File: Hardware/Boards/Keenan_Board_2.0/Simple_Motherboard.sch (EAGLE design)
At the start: 109 parts, among them J1 AVR_SPI_PRG_6PTH, U1 WIZ811MJ, U1_MUX 74HC4052D,653, U2 ATMEGA328P_PDIP, U2_MUX 74HC4052D,653, U3_MUX 74HC4052D,653, U4_MUX 74HC4052D,653, U5_MUX 74HC4052D,653, U7_MUX 74HC4052D,653, Y1 16MHz

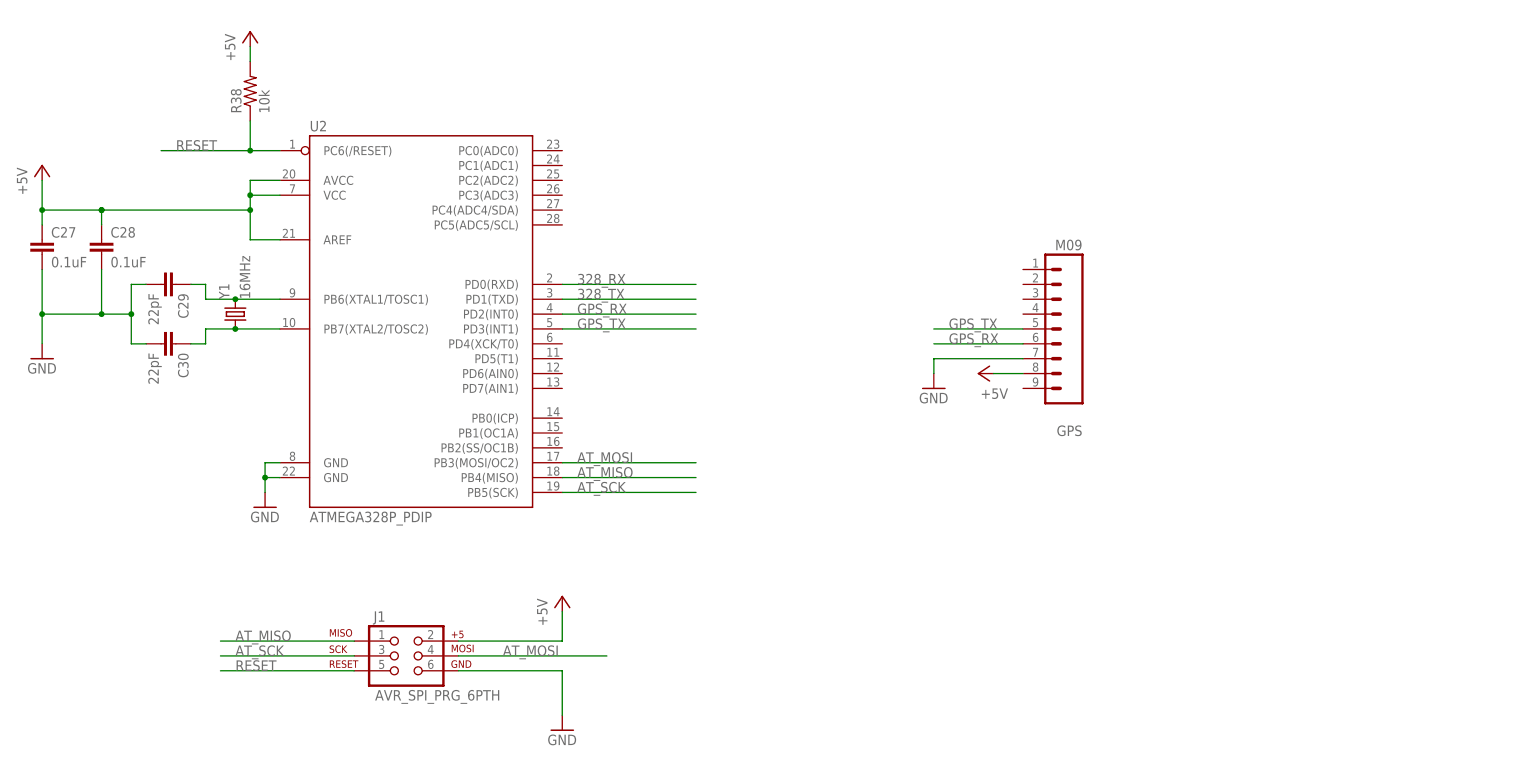
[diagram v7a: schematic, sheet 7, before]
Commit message: Added Bluetooth to schematic
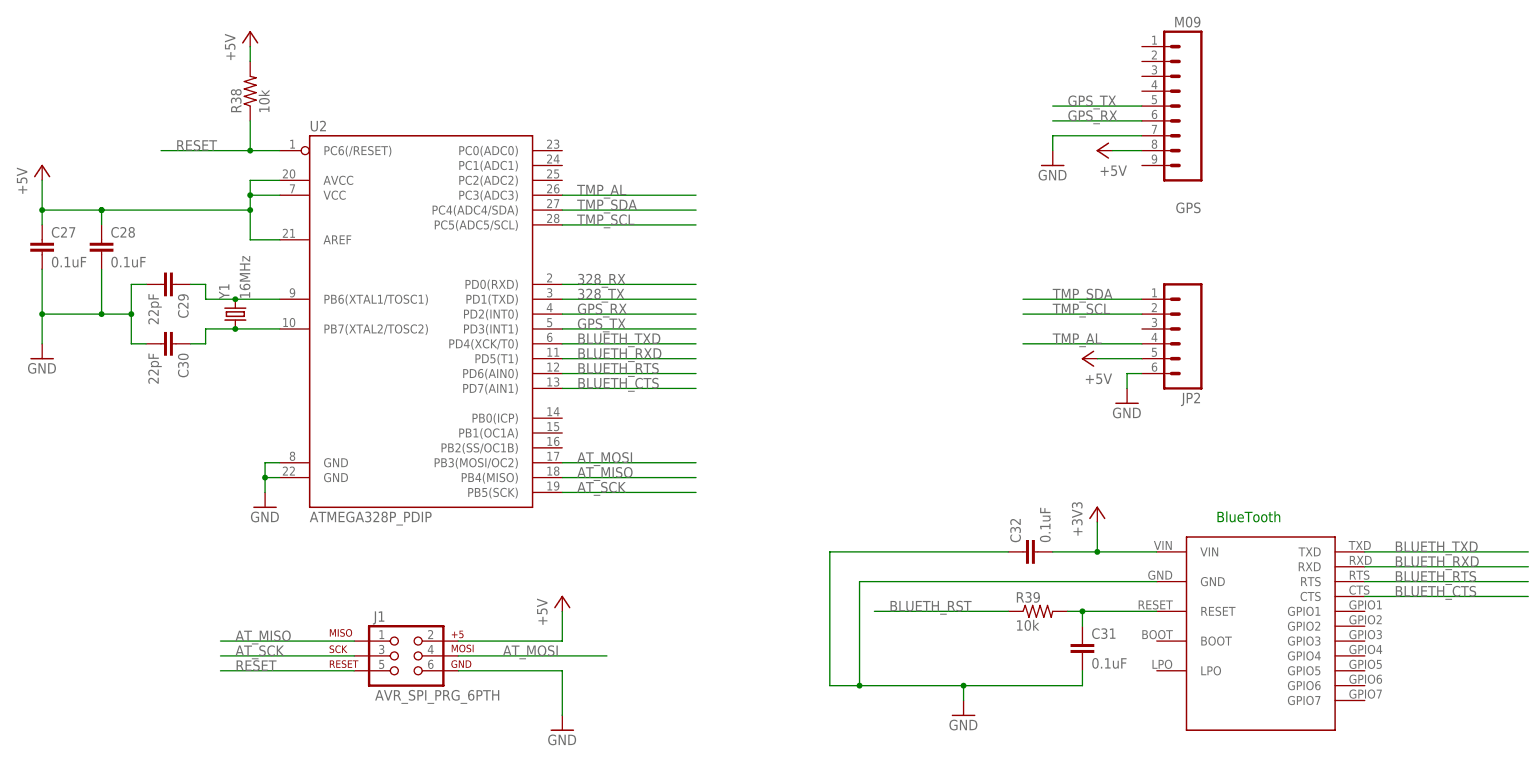
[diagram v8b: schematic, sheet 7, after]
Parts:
- added BLUETOOTH: SPBT2632C2A, SPBT2632C2A:SPBT2632C2A
- added C31, C32: 0.1uF, SparkFun-Passives:CAP1206
- added JP2: (no value), SparkFun-Connectors:M06LONGPADS
- added R39: 10k, SparkFun-Passives:RESISTOR1206
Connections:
- new net BLUETH_CTS: BLUETOOTH.CTS, U2.PD7(AIN1)
- new net BLUETH_RST: R39.1
- new net BLUETH_RTS: BLUETOOTH.RTS, U2.PD6(AIN0)
- new net BLUETH_RXD: BLUETOOTH.RXD, U2.PD5(T1)
- new net BLUETH_TXD: BLUETOOTH.TXD, U2.PD4(XCK/T0)
- new net N$58: BLUETOOTH.RESET, C31.1, R39.2
- new net TMP_AL: JP2.4, U2.PC3(ADC3)
- new net TMP_SCL: JP2.2, U2.PC5(ADC5/SCL)
- new net TMP_SDA: JP2.1, U2.PC4(ADC4/SDA)
- net +3V3: now also BLUETOOTH.VIN, C32.2
- net +5V: now also JP2.5
- net GND: now also BLUETOOTH.GND, C31.2, C32.1, JP2.6
- net GPS_RX: now also U5_MUX.2Y3
- net GPS_TX: now also U5_MUX.1Y3
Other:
- note added: "BlueTooth"
- moved on the sheet: GPS
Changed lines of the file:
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@@
 <part name="P+31" library="supply1" deviceset="+5V" device=""/>
 <part name="GND36" library="supply1" deviceset="GND" device=""/>
+<part name="JP2" library="SparkFun-Connectors" deviceset="M06" device="LONGPADS"/>
+<part name="GND37" library="supply1" deviceset="GND" device=""/>
+<part name="P+32" library="supply1" deviceset="+5V" device=""/>
+<part name="BLUETOOTH" library="SPBT2632C2A" deviceset="SPBT2632C2A" device=""/>
+<part name="GND38" library="supply1" deviceset="GND" device=""/>
+<part name="+3V33" library="supply1" deviceset="+3V3" device=""/>
+<part name="C31" library="SparkFun-Passives" deviceset="CAP" device="1206" value="0.1uF"/>
+<part name="R39" library="SparkFun-Passives" deviceset="RESISTOR" device="1206" value="10k"/>
+<part name="C32" library="SparkFun-Passives" deviceset="CAP" device="1206" value="0.1uF"/>
 </parts>
 <sheets>
@@
 </segment>
 </net>
+<net name="GPS_RX" class="0">
+<segment>
+<pinref part="U5_MUX" gate="A" pin="2Y3"/>
+<wire x1="17.78" y1="-43.18" x2="38.1" y2="-43.18" width="0.1524" layer="91"/>
+<label x="20.32" y="-43.18" size="1.778" layer="95"/>
+</segment>
+</net>
+<net name="GPS_TX" class="0">
+<segment>
+<pinref part="U5_MUX" gate="A" pin="1Y3"/>
+<wire x1="17.78" y1="-30.48" x2="38.1" y2="-30.48" width="0.1524" layer="91"/>
+<label x="20.32" y="-30.48" size="1.778" layer="95"/>
+</segment>
+</net>
 </nets>
 </sheet>
@@
 <description>Sensors</description>
 <plain>
+<text x="137.16" y="-38.1" size="1.778" layer="91">BlueTooth</text>
 </plain>
 <instances>
@@
 <instance part="P+30" gate="1" x="25.4" y="-50.8"/>
 <instance part="GND35" gate="1" x="25.4" y="-73.66"/>
-<instance part="GPS" gate="G$1" x="114.3" y="-5.08" rot="R180"/>
-<instance part="P+31" gate="1" x="96.52" y="-12.7" rot="R90"/>
-<instance part="GND36" gate="1" x="88.9" y="-15.24"/>
+<instance part="GPS" gate="G$1" x="134.62" y="33.02" rot="R180"/>
+<instance part="P+31" gate="1" x="116.84" y="25.4" rot="R90"/>
+<instance part="GND36" gate="1" x="109.22" y="22.86"/>
+<instance part="JP2" gate="G$1" x="129.54" y="-5.08" rot="R180"/>
+<instance part="GND37" gate="1" x="121.92" y="-17.78"/>
+<instance part="P+32" gate="1" x="114.3" y="-10.16" rot="R90"/>
+<instance part="BLUETOOTH" gate="G$1" x="144.78" y="-55.88"/>
+<instance part="GND38" gate="1" x="93.98" y="-71.12"/>
+<instance part="+3V33" gate="G$1" x="116.84" y="-35.56"/>
+<instance part="C31" gate="G$1" x="114.3" y="-60.96"/>
+<instance part="R39" gate="G$1" x="106.68" y="-53.34"/>
+<instance part="C32" gate="G$1" x="106.68" y="-43.18" rot="R90"/>
 </instances>
 <busses>
@@
 <segment>
 <pinref part="GND36" gate="1" pin="GND"/>
-<wire x1="88.9" y1="-12.7" x2="88.9" y2="-10.16" width="0.1524" layer="91"/>
+<wire x1="109.22" y1="25.4" x2="109.22" y2="27.94" width="0.1524" layer="91"/>
 <pinref part="GPS" gate="G$1" pin="7"/>
-<wire x1="88.9" y1="-10.16" x2="104.14" y2="-10.16" width="0.1524" layer="91"/>
+<wire x1="109.22" y1="27.94" x2="124.46" y2="27.94" width="0.1524" layer="91"/>
+</segment>
+<segment>
+<pinref part="JP2" gate="G$1" pin="6"/>
+<pinref part="GND37" gate="1" pin="GND"/>
+<wire x1="124.46" y1="-12.7" x2="121.92" y2="-12.7" width="0.1524" layer="91"/>
+<wire x1="121.92" y1="-12.7" x2="121.92" y2="-15.24" width="0.1524" layer="91"/>
+</segment>
+<segment>
+<pinref part="BLUETOOTH" gate="G$1" pin="GND"/>
+<wire x1="127" y1="-48.26" x2="76.2" y2="-48.26" width="0.1524" layer="91"/>
+<wire x1="76.2" y1="-48.26" x2="76.2" y2="-66.04" width="0.1524" layer="91"/>
+<pinref part="C31" gate="G$1" pin="2"/>
+<wire x1="114.3" y1="-63.5" x2="114.3" y2="-66.04" width="0.1524" layer="91"/>
+<wire x1="114.3" y1="-66.04" x2="93.98" y2="-66.04" width="0.1524" layer="91"/>
+<pinref part="GND38" gate="1" pin="GND"/>
+<wire x1="93.98" y1="-66.04" x2="76.2" y2="-66.04" width="0.1524" layer="91"/>
+<wire x1="93.98" y1="-68.58" x2="93.98" y2="-66.04" width="0.1524" layer="91"/>
+<junction x="93.98" y="-66.04"/>
+<pinref part="C32" gate="G$1" pin="1"/>
+<wire x1="101.6" y1="-43.18" x2="71.12" y2="-43.18" width="0.1524" layer="91"/>
+<wire x1="71.12" y1="-43.18" x2="71.12" y2="-66.04" width="0.1524" layer="91"/>
+<wire x1="71.12" y1="-66.04" x2="76.2" y2="-66.04" width="0.1524" layer="91"/>
+<junction x="76.2" y="-66.04"/>
 </segment>
 </net>
@@
 <pinref part="P+31" gate="1" pin="+5V"/>
 <pinref part="GPS" gate="G$1" pin="8"/>
-<wire x1="99.06" y1="-12.7" x2="104.14" y2="-12.7" width="0.1524" layer="91"/>
+<wire x1="119.38" y1="25.4" x2="124.46" y2="25.4" width="0.1524" layer="91"/>
+</segment>
+<segment>
+<pinref part="P+32" gate="1" pin="+5V"/>
+<pinref part="JP2" gate="G$1" pin="5"/>
+<wire x1="116.84" y1="-10.16" x2="124.46" y2="-10.16" width="0.1524" layer="91"/>
 </segment>
 </net>
@@
 <segment>
 <pinref part="GPS" gate="G$1" pin="6"/>
-<wire x1="104.14" y1="-7.62" x2="88.9" y2="-7.62" width="0.1524" layer="91"/>
-<label x="91.44" y="-7.62" size="1.778" layer="95"/>
+<wire x1="124.46" y1="30.48" x2="109.22" y2="30.48" width="0.1524" layer="91"/>
+<label x="111.76" y="30.48" size="1.778" layer="95"/>
 </segment>
 <segment>
@@
 <segment>
 <pinref part="GPS" gate="G$1" pin="5"/>
-<wire x1="104.14" y1="-5.08" x2="88.9" y2="-5.08" width="0.1524" layer="91"/>
-<label x="91.44" y="-5.08" size="1.778" layer="95"/>
+<wire x1="124.46" y1="33.02" x2="109.22" y2="33.02" width="0.1524" layer="91"/>
+<label x="111.76" y="33.02" size="1.778" layer="95"/>
 </segment>
 <segment>
@@
 </segment>
 </net>
+<net name="TMP_SDA" class="0">
+<segment>
+<pinref part="JP2" gate="G$1" pin="1"/>
+<wire x1="124.46" y1="0" x2="104.14" y2="0" width="0.1524" layer="91"/>
+<label x="109.22" y="0" size="1.778" layer="95"/>
+</segment>
+<segment>
+<pinref part="U2" gate="G$1" pin="PC4(ADC4/SDA)"/>
+<wire x1="25.4" y1="15.24" x2="48.26" y2="15.24" width="0.1524" layer="91"/>
+<label x="27.94" y="15.24" size="1.778" layer="95"/>
+</segment>
+</net>
+<net name="TMP_AL" class="0">
+<segment>
+<pinref part="JP2" gate="G$1" pin="4"/>
+<wire x1="124.46" y1="-7.62" x2="104.14" y2="-7.62" width="0.1524" layer="91"/>
+<label x="109.22" y="-7.62" size="1.778" layer="95"/>
+</segment>
+<segment>
+<pinref part="U2" gate="G$1" pin="PC3(ADC3)"/>
+<wire x1="25.4" y1="17.78" x2="48.26" y2="17.78" width="0.1524" layer="91"/>
+<label x="27.94" y="17.78" size="1.778" layer="95"/>
+</segment>
+</net>
+<net name="TMP_SCL" class="0">
+<segment>
+<pinref part="JP2" gate="G$1" pin="2"/>
+<wire x1="124.46" y1="-2.54" x2="104.14" y2="-2.54" width="0.1524" layer="91"/>
+<label x="109.22" y="-2.54" size="1.778" layer="95"/>
+</segment>
+<segment>
+<pinref part="U2" gate="G$1" pin="PC5(ADC5/SCL)"/>
+<wire x1="25.4" y1="12.7" x2="48.26" y2="12.7" width="0.1524" layer="91"/>
+<label x="27.94" y="12.7" size="1.778" layer="95"/>
+</segment>
+</net>
+<net name="+3V3" class="0">
+<segment>
+<pinref part="+3V33" gate="G$1" pin="+3V3"/>
+<wire x1="116.84" y1="-38.1" x2="116.84" y2="-43.18" width="0.1524" layer="91"/>
+<pinref part="BLUETOOTH" gate="G$1" pin="VIN"/>
+<wire x1="116.84" y1="-43.18" x2="127" y2="-43.18" width="0.1524" layer="91"/>
+<pinref part="C32" gate="G$1" pin="2"/>
+<wire x1="116.84" y1="-43.18" x2="109.22" y2="-43.18" width="0.1524" layer="91"/>
+<junction x="116.84" y="-43.18"/>
+</segment>
+</net>
+<net name="BLUETH_TXD" class="0">
+<segment>
+<pinref part="BLUETOOTH" gate="G$1" pin="TXD"/>
+<wire x1="162.56" y1="-43.18" x2="190.5" y2="-43.18" width="0.1524" layer="91"/>
+<label x="167.64" y="-43.18" size="1.778" layer="95"/>
+</segment>
+<segment>
+<pinref part="U2" gate="G$1" pin="PD4(XCK/T0)"/>
+<wire x1="25.4" y1="-7.62" x2="48.26" y2="-7.62" width="0.1524" layer="91"/>
+<label x="27.94" y="-7.62" size="1.778" layer="95"/>
+</segment>
+</net>
+<net name="BLUETH_RXD" class="0">
+<segment>
+<pinref part="BLUETOOTH" gate="G$1" pin="RXD"/>
+<wire x1="162.56" y1="-45.72" x2="190.5" y2="-45.72" width="0.1524" layer="91"/>
+<label x="167.64" y="-45.72" size="1.778" layer="95"/>
+</segment>
+<segment>
+<pinref part="U2" gate="G$1" pin="PD5(T1)"/>
+<wire x1="25.4" y1="-10.16" x2="48.26" y2="-10.16" width="0.1524" layer="91"/>
+<label x="27.94" y="-10.16" size="1.778" layer="95"/>
+</segment>
+</net>
+<net name="BLUETH_RTS" class="0">
+<segment>
+<pinref part="BLUETOOTH" gate="G$1" pin="RTS"/>
+<wire x1="162.56" y1="-48.26" x2="190.5" y2="-48.26" width="0.1524" layer="91"/>
+<label x="167.64" y="-48.26" size="1.778" layer="95"/>
+</segment>
+<segment>
+<pinref part="U2" gate="G$1" pin="PD6(AIN0)"/>
+<wire x1="25.4" y1="-12.7" x2="48.26" y2="-12.7" width="0.1524" layer="91"/>
+<label x="27.94" y="-12.7" size="1.778" layer="95"/>
+</segment>
+</net>
+<net name="BLUETH_CTS" class="0">
+<segment>
+<pinref part="BLUETOOTH" gate="G$1" pin="CTS"/>
+<wire x1="162.56" y1="-50.8" x2="190.5" y2="-50.8" width="0.1524" layer="91"/>
+<label x="167.64" y="-50.8" size="1.778" layer="95"/>
+</segment>
+<segment>
+<pinref part="U2" gate="G$1" pin="PD7(AIN1)"/>
+<wire x1="25.4" y1="-15.24" x2="48.26" y2="-15.24" width="0.1524" layer="91"/>
+<label x="27.94" y="-15.24" size="1.778" layer="95"/>
+</segment>
+</net>
+<net name="BLUETH_RST" class="0">
+<segment>
+<pinref part="R39" gate="G$1" pin="1"/>
+<wire x1="101.6" y1="-53.34" x2="78.74" y2="-53.34" width="0.1524" layer="91"/>
+<label x="81.28" y="-53.34" size="1.778" layer="95"/>
+</segment>
+</net>
+<net name="N$58" class="0">
+<segment>
+<pinref part="R39" gate="G$1" pin="2"/>
+<pinref part="BLUETOOTH" gate="G$1" pin="RESET"/>
+<wire x1="111.76" y1="-53.34" x2="114.3" y2="-53.34" width="0.1524" layer="91"/>
+<pinref part="C31" gate="G$1" pin="1"/>
+<wire x1="114.3" y1="-53.34" x2="127" y2="-53.34" width="0.1524" layer="91"/>
+<wire x1="114.3" y1="-55.88" x2="114.3" y2="-53.34" width="0.1524" layer="91"/>
+<junction x="114.3" y="-53.34"/>
+</segment>
+</net>
